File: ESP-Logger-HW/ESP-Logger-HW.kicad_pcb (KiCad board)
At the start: 2 copper layers, 2 parts

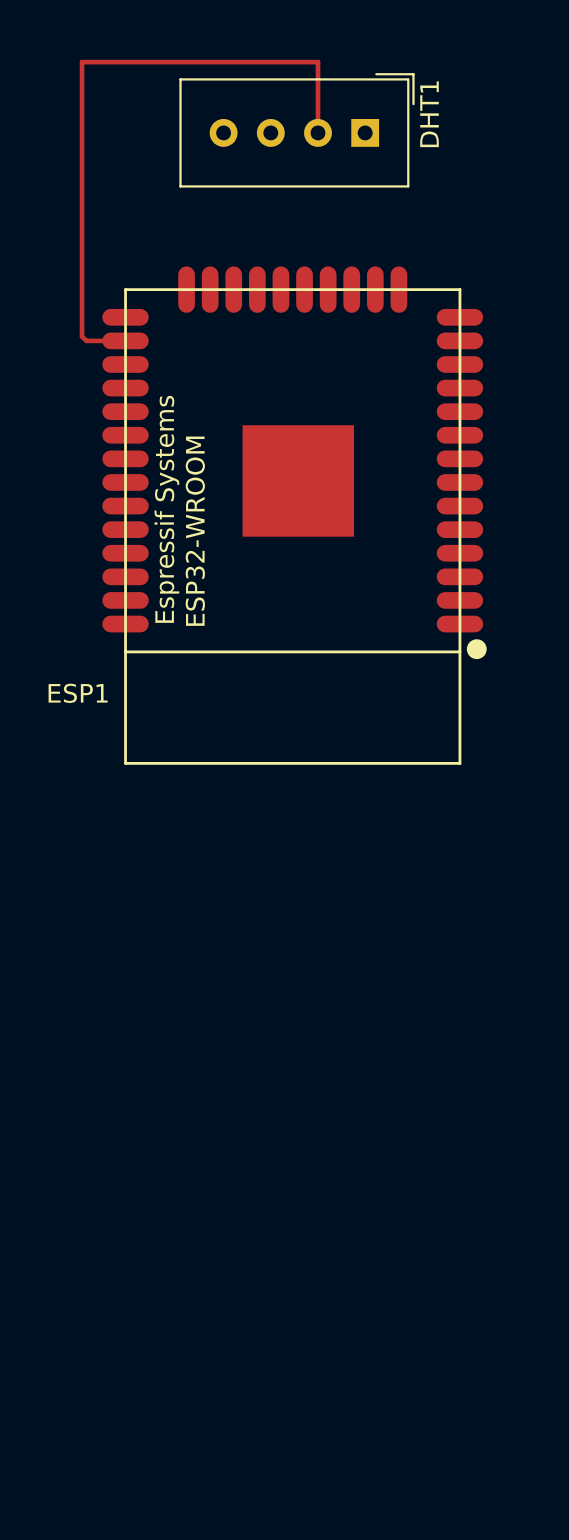
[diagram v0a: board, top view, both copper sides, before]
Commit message: First complete PCB
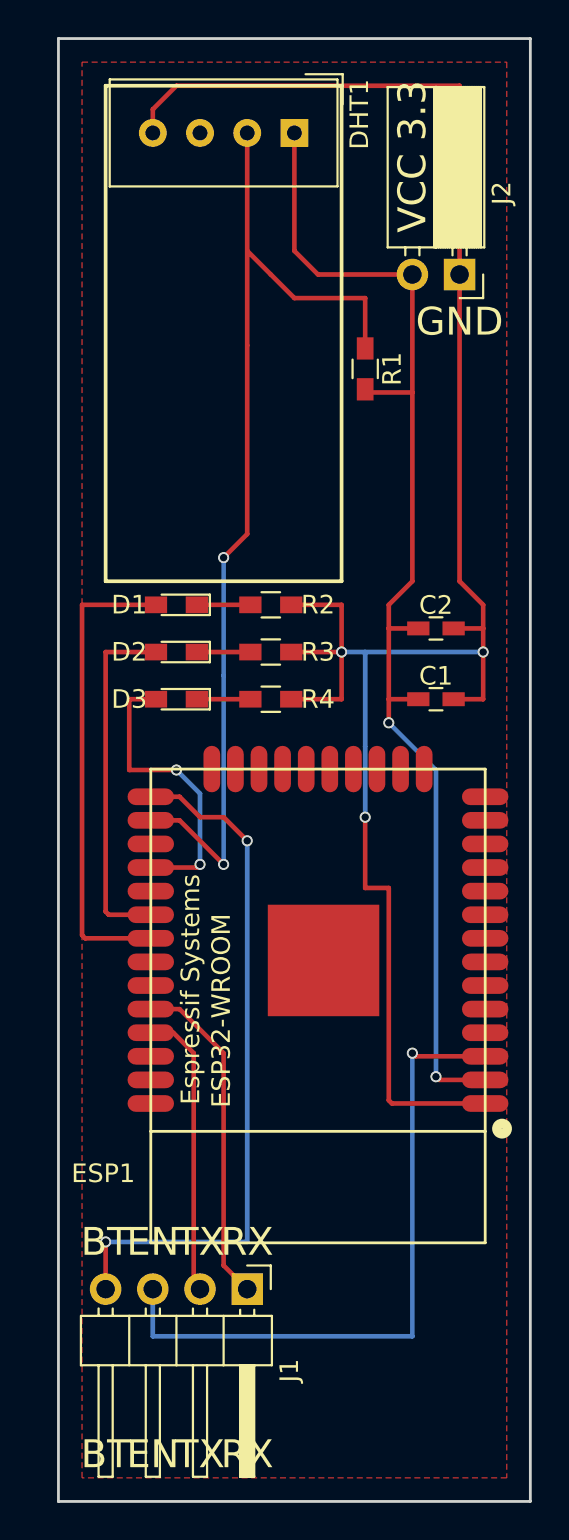
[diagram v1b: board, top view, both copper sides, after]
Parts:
- added C1: 0.1uF, Capacitors_SMD:C_0603_HandSoldering, F.Cu at (58.4, 62.2)
- added C2: 10uF, Capacitors_SMD:C_0603_HandSoldering, F.Cu at (58.4, 58.4)
- added D1: LED, LEDs:LED_0603_HandSoldering, F.Cu at (44.5, 57.1)
- added D2: LED, LEDs:LED_0603_HandSoldering, F.Cu at (44.5, 59.7)
- added D3: LED, LEDs:LED_0603_HandSoldering, F.Cu at (44.5, 62.2)
- added J1: Conn_01x04_Male, Pin_Headers:Pin_Header_Angled_1x04_Pitch2.54mm, F.Cu at (48.3, 94.0)
- added J2: Conn_01x02_Female, Socket_Strips:Socket_Strip_Angled_1x02_Pitch2.54mm, F.Cu at (59.7, 39.4)
- added R1: 1K, Resistors_SMD:R_0603_HandSoldering, F.Cu at (54.6, 44.5)
- added R2: 220, Resistors_SMD:R_0603_HandSoldering, F.Cu at (49.5, 57.1)
- added R3: 220, Resistors_SMD:R_0603_HandSoldering, F.Cu at (49.5, 59.7)
- added R4: 220, Resistors_SMD:R_0603_HandSoldering, F.Cu at (49.5, 62.2)
- moved ESP1 25.8 mm to (52.1, 78.7)
- moved DHT1 3.81 mm to (50.8, 31.8)
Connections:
- ESP1 pad 25: Net-(ESP1-Pad25) -> /BOOT
- ESP1 pad 39: Net-(ESP1-Pad39) -> GND
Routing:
- net GND: track 0.00 -> 106.5 mm, vias 0 -> 3
- net VCC: track 0.00 -> 66.5 mm, vias 0 -> 2
- net /BOOT: track 0.00 -> 37.9 mm, vias 0 -> 2
- net Net-(ESP1-Pad3): track 0.00 -> 35.7 mm, vias 0 -> 1
- net Net-(D1-Pad2): track 0.00 -> 25.5 mm
- net Net-(DHT1-Pad2): track 33.7 -> 54.9 mm, vias 0 -> 2
- net Net-(D2-Pad2): track 0.00 -> 19.2 mm
- net Net-(ESP1-Pad34): track 0.00 -> 18.1 mm
- net Net-(D3-Pad2): track 0.00 -> 16.1 mm, vias 0 -> 2
- net Net-(ESP1-Pad35): track 0.00 -> 15.6 mm
- net Net-(D3-Pad1): track 0.00 -> 2.88 mm
- net Net-(D2-Pad1): track 0.00 -> 2.88 mm
- net Net-(D1-Pad1): track 0.00 -> 2.88 mm
- added copper zone on F.Cu, net GND
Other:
- board outline added: 25.4 x 78.7 mm
- rule pad_to_mask_clearance: 0.2 -> 0.1
- rule trace_min: 0.2 -> 0.25
- board text added: "BT"
- board text added: "EN"
- board text added: "GND"
- board text added: "RX"
- board text added: "TX"
- board text added: "VCC 3.3"

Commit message: Update the Pcb: Added the RC-Delay circuit that I forgot on the first prototype
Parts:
- added C3: 1uF, Capacitors_SMD:C_0603_HandSoldering, F.Cu at (61.0, 52.1)
- added R5: 10K, Resistors_SMD:R_0603_HandSoldering, F.Cu at (55.9, 52.1)
- J1: footprint Pin_Headers:Pin_Header_Angled_1x04_Pitch2.54mm -> Connectors_JST:JST_XH_B04B-XH-A_04x2.50mm_Straight
- J2: footprint Socket_Strips:Socket_Strip_Angled_1x02_Pitch2.54mm -> Connectors_JST:JST_XH_B02B-XH-A_02x2.50mm_Straight
- moved J1 10.1 mm to (58.3, 95.2), turned to 180 degrees
- moved J2 3.81 mm to (59.7, 35.6), turned to 180 degrees
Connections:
- net /BOOT renamed Net-(ESP1-Pad25)
- ESP1 pad 38: Net-(ESP1-Pad38) -> GND
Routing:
- net GND: track 106.5 -> 161.4 mm
- net Net-(C3-Pad1): track 35.7 -> 68.7 mm, vias 1 -> 5
- net Net-(ESP1-Pad34): track 18.1 -> 32.0 mm, vias 0 -> 3
- net Net-(ESP1-Pad35): track 15.6 -> 29.4 mm, vias 0 -> 4
- net Net-(ESP1-Pad25): track 37.9 -> 31.9 mm, vias 2 -> 0
- net VCC: track 66.5 -> 71.7 mm
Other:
- board size 25.4 x 78.7 mm -> 25.4 x 73.7 mm

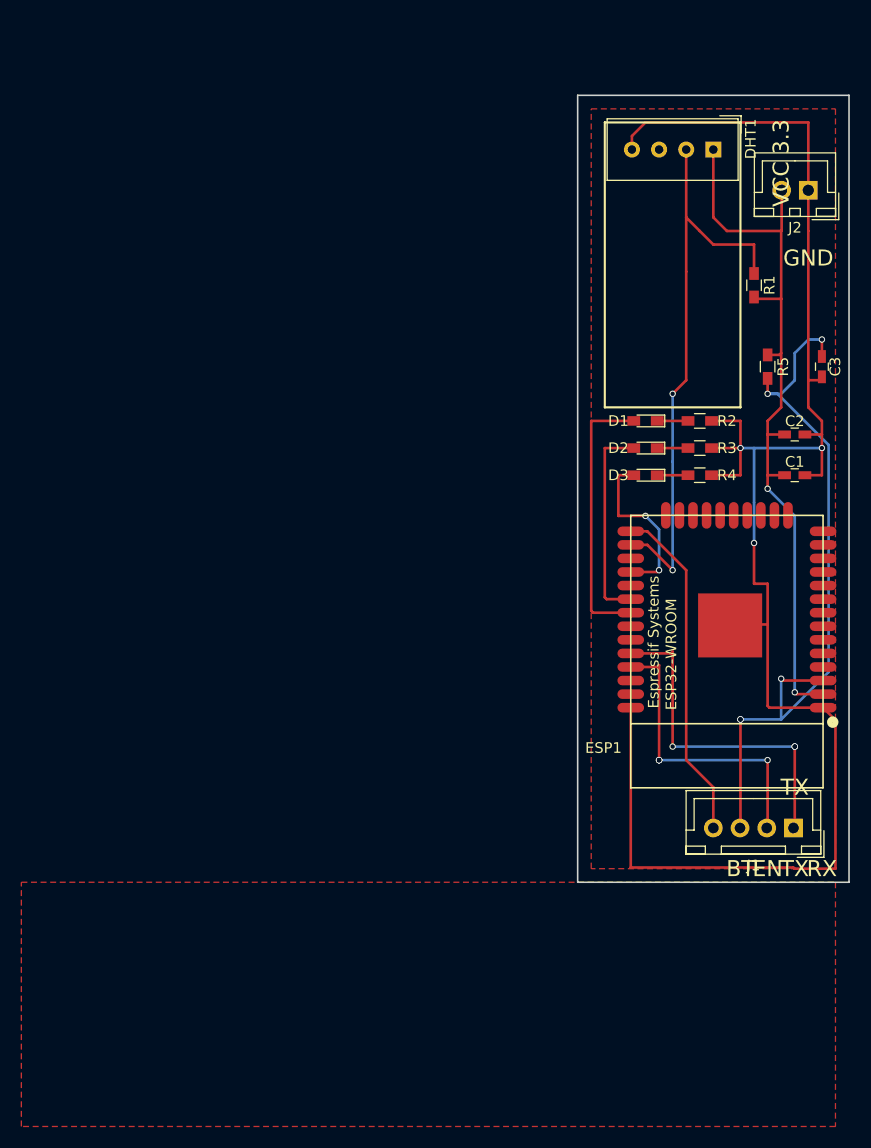
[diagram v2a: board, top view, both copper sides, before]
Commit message: New 30x40 mm small Pcb layout
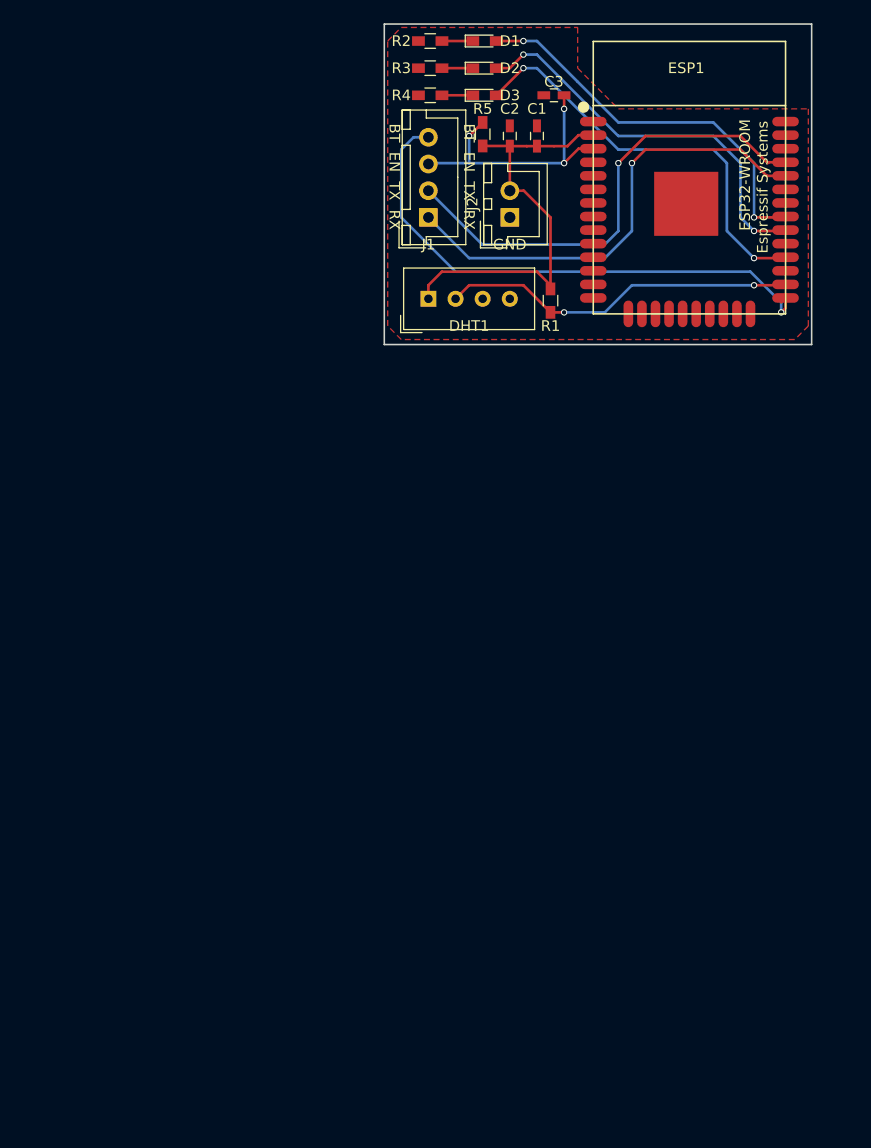
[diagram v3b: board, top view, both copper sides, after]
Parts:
- moved J1 66.6 mm to (24.1, 38.1), turned to 90 degrees
- moved ESP1 44.5 mm to (48.6, 34.4), turned to 180 degrees
- moved R2 43.6 mm to (24.3, 21.6), turned to 180 degrees
- moved R3 43.6 mm to (24.3, 24.1), turned to 180 degrees
- moved R4 43.6 mm to (24.3, 26.7), turned to 180 degrees
- moved C1 39.9 mm to (34.3, 30.5), turned to 90 degrees
- moved C2 38.6 mm to (31.8, 30.5), turned to 90 degrees
- moved D1 38.6 mm to (29.4, 21.6), turned to 0 degrees
- moved D2 38.6 mm to (29.4, 24.1), turned to 0 degrees
- moved D3 38.6 mm to (29.4, 26.7), turned to 0 degrees
- moved C3 35.7 mm to (35.9, 26.7), turned to 180 degrees
- moved R5 34.4 mm to (29.2, 30.3), turned to 90 degrees
- moved DHT1 30.1 mm to (24.1, 45.7), turned to 90 degrees
- moved J2 28.1 mm to (31.8, 38.1), turned to 90 degrees
- moved R1 19.1 mm to (35.6, 45.9), turned to 90 degrees
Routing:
- net GND: track 161.4 -> 0.43 mm, vias 3 -> 0
- net Net-(C3-Pad1): track 68.7 -> 26.8 mm, vias 5 -> 3
- net VCC: track 71.7 -> 40.6 mm, vias 2 -> 0
- net Net-(D3-Pad2): track 16.1 -> 39.2 mm
- net Net-(DHT1-Pad2): track 54.9 -> 33.6 mm
- net Net-(ESP1-Pad25): track 31.9 -> 51.3 mm, vias 0 -> 1
- net Net-(D2-Pad2): track 19.2 -> 37.5 mm, vias 0 -> 2
- net Net-(ESP1-Pad35): track 29.4 -> 44.5 mm, vias 4 -> 1
- net Net-(ESP1-Pad34): track 32.0 -> 44.0 mm, vias 3 -> 1
- net Net-(D1-Pad2): track 25.5 -> 36.9 mm, vias 0 -> 2
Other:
- board size 25.4 x 73.7 mm -> 40 x 30 mm
- board text added: "BT EN TX RX"
- board text removed: "BT"
- board text removed: "EN"
- board text removed: "RX"
- board text removed: "TX"
- board text removed: "VCC 3.3"

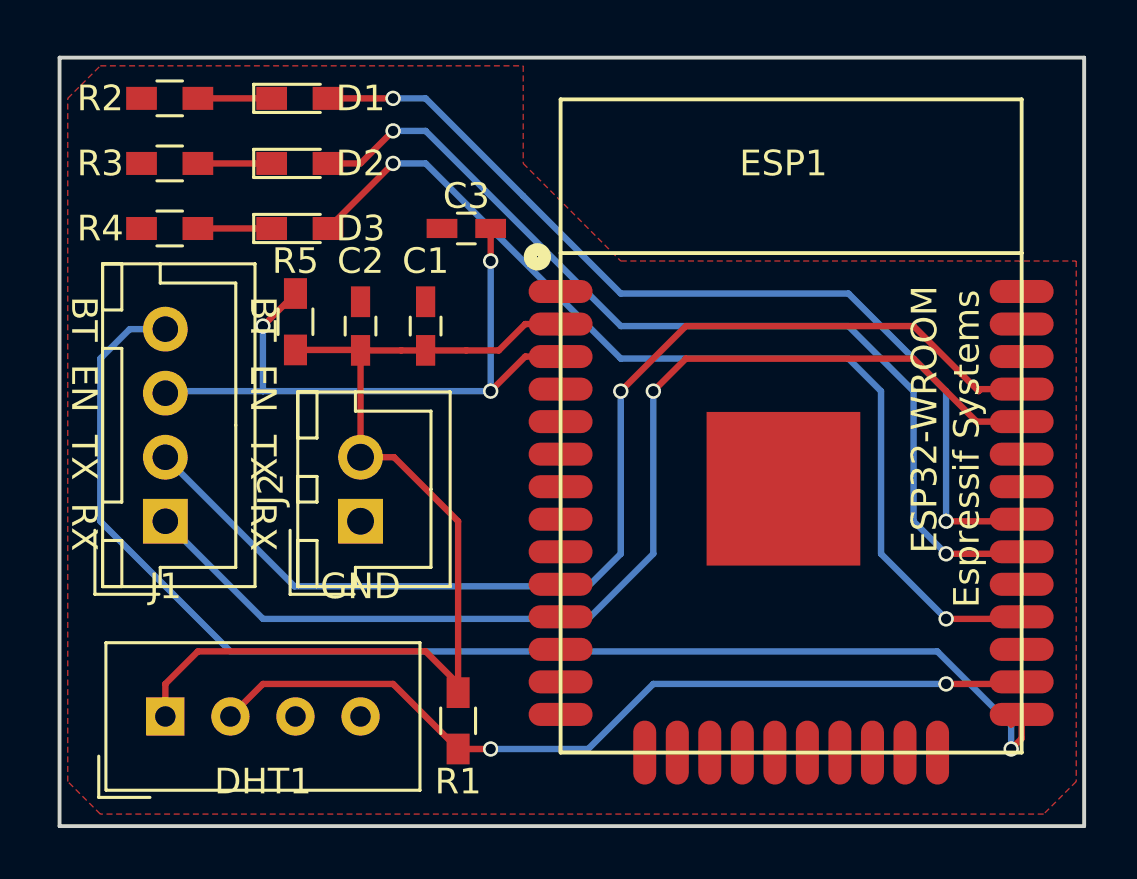
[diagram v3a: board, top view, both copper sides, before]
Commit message: Update PCB and Gerber: Add USB power supply and voltage regulator
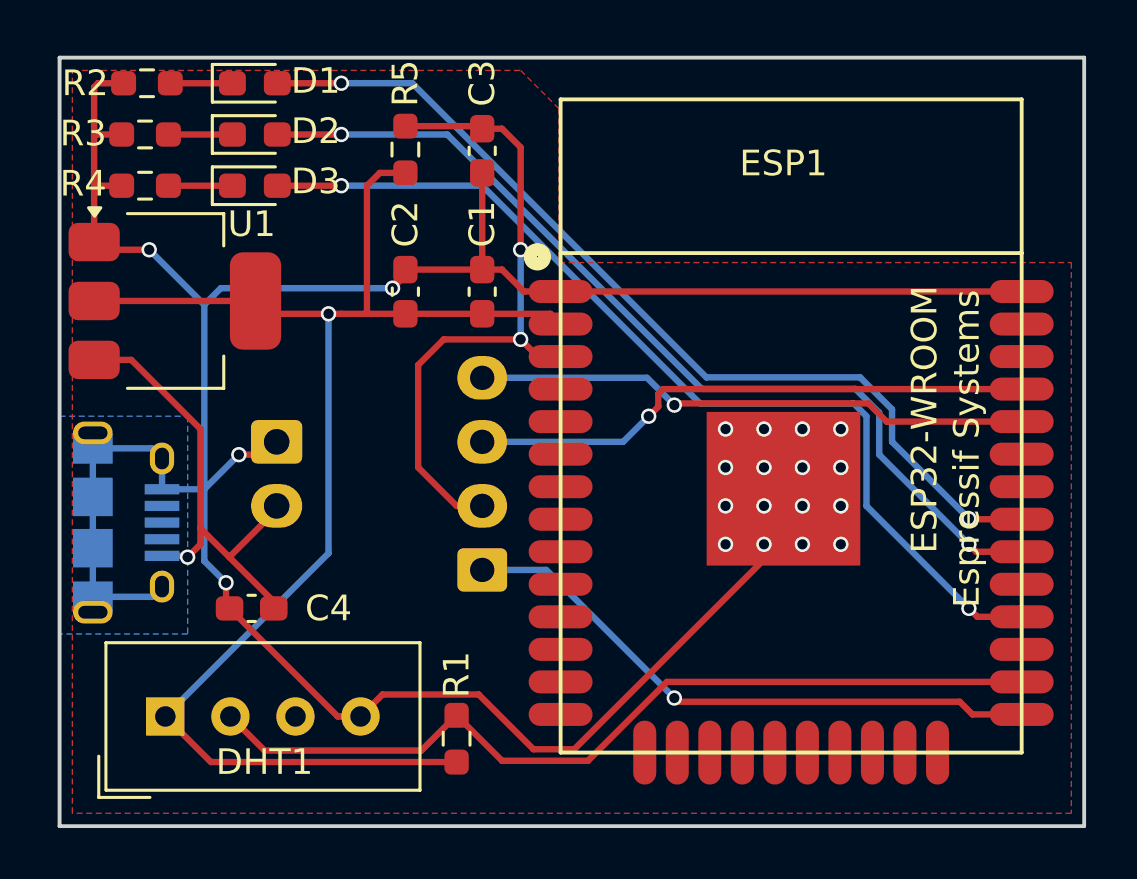
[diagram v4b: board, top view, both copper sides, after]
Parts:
- added C4: 0.1uF, Capacitor_SMD:C_0603_1608Metric_Pad1.08x0.95mm_HandSolder, F.Cu at (27.5, 41.5)
- added J3: USB, Connector_USB:USB_Micro-B_Amphenol_10118194_Horizontal, B.Cu at (22.6, 38.1)
- added U1: LD33V, Package_TO_SOT_SMD:SOT-223-3_TabPin2, F.Cu at (24.5, 29.5)
- C1, C2, C3: footprint Capacitors_SMD:C_0603_HandSoldering -> Capacitor_SMD:C_0603_1608Metric_Pad1.08x0.95mm_HandSolder
- D1, D2, D3: footprint LEDs:LED_0603_HandSoldering -> LED_SMD:LED_0603_1608Metric_Pad1.05x0.95mm_HandSolder
- J1: footprint Connectors_JST:JST_XH_B04B-XH-A_04x2.50mm_Straight -> Connector_JST:JST_XH_B4B-XH-A_1x04_P2.50mm_Vertical; moved to B.Cu
- J2: value Conn_01x02_Female -> PWR; footprint Connectors_JST:JST_XH_B02B-XH-A_02x2.50mm_Straight -> Connector_JST:JST_XH_B2B-XH-A_1x02_P2.50mm_Vertical; moved to B.Cu
- R1, R2, R3, R4, R5: footprint Resistors_SMD:R_0603_HandSoldering -> Resistor_SMD:R_0603_1608Metric_Pad0.98x0.95mm_HandSolder
- moved J1 12.5 mm to (36.5, 40.0)
- moved R5 7.97 mm to (33.5, 23.6)
- moved J2 4.51 mm to (28.5, 35.0), turned to -90 degrees
- moved C3 3.10 mm to (36.5, 23.6), turned to -90 degrees
- moved C1 2.59 mm to (36.5, 29.1)
- moved D3 2.42 mm to (27.6, 25.0)
- moved C2 2.21 mm to (33.5, 29.1)
- moved D2 2.09 mm to (27.6, 23.0)
- moved R4 1.93 mm to (23.3, 25.0)
- moved D1 1.85 mm to (27.6, 21.0)
- moved R3 1.48 mm to (23.3, 23.0)
- moved R2 1.07 mm to (23.4, 21.0)
- moved R1 0.70 mm to (35.5, 46.6), turned to -90 degrees
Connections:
- C3 pad 1: Net-(C3-Pad1) -> Net-(ESP1-EN)
- DHT1 pad 3: Net-(DHT1-Pad3) -> unconnected-(DHT1-NC-Pad3)
- ESP1 pad 10: Net-(ESP1-Pad10) -> unconnected-(ESP1-IO25-Pad10)
- ESP1 pad 11: Net-(ESP1-Pad11) -> unconnected-(ESP1-IO26-Pad11)
- ESP1 pad 12: Net-(ESP1-Pad12) -> unconnected-(ESP1-IO27-Pad12)
- ESP1 pad 13: Net-(ESP1-Pad13) -> unconnected-(ESP1-IO14-Pad13)
- ESP1 pad 14: Net-(ESP1-Pad14) -> unconnected-(ESP1-IO12-Pad14)
- ESP1 pad 15: Net-(ESP1-Pad15) -> unconnected-(ESP1-GND-Pad15)
- ESP1 pad 16: Net-(ESP1-Pad16) -> unconnected-(ESP1-IO13-Pad16)
- ESP1 pad 17: Net-(ESP1-Pad17) -> unconnected-(ESP1-SD2-Pad17)
- ESP1 pad 18: Net-(ESP1-Pad18) -> unconnected-(ESP1-SD3-Pad18)
- ESP1 pad 19: Net-(ESP1-Pad19) -> unconnected-(ESP1-CMD-Pad19)
- ESP1 pad 20: Net-(ESP1-Pad20) -> unconnected-(ESP1-CLK-Pad20)
- ESP1 pad 21: Net-(ESP1-Pad21) -> unconnected-(ESP1-SDO-Pad21)
- ESP1 pad 22: Net-(ESP1-Pad22) -> unconnected-(ESP1-SD1-Pad22)
- ESP1 pad 23: Net-(ESP1-Pad23) -> unconnected-(ESP1-IO15-Pad23)
- ESP1 pad 24: Net-(ESP1-Pad24) -> unconnected-(ESP1-IO2-Pad24)
- ESP1 pad 25: Net-(ESP1-Pad25) -> Net-(ESP1-IO0)
- ESP1 pad 27: Net-(ESP1-Pad27) -> unconnected-(ESP1-IO16-Pad27)
- ESP1 pad 29: Net-(ESP1-Pad29) -> unconnected-(ESP1-IO5-Pad29)
- ESP1 pad 3: Net-(C3-Pad1) -> Net-(ESP1-EN)
- ESP1 pad 32: Net-(ESP1-Pad32) -> unconnected-(ESP1-NC-Pad32)
- ESP1 pad 33: Net-(ESP1-Pad33) -> unconnected-(ESP1-IO21-Pad33)
- ESP1 pad 34: Net-(ESP1-Pad34) -> Net-(ESP1-RXD0)
- ESP1 pad 35: Net-(ESP1-Pad35) -> Net-(ESP1-TXD0)
- ESP1 pad 36: Net-(ESP1-Pad36) -> unconnected-(ESP1-IO22-Pad36)
- ESP1 pad 37: Net-(ESP1-Pad37) -> unconnected-(ESP1-IO23-Pad37)
- ESP1 pad 4: Net-(ESP1-Pad4) -> unconnected-(ESP1-SENSOR_VP-Pad4)
- ESP1 pad 5: Net-(ESP1-Pad5) -> unconnected-(ESP1-SENSOR_VN-Pad5)
- ESP1 pad 6: Net-(ESP1-Pad6) -> unconnected-(ESP1-IO34-Pad6)
- ESP1 pad 7: Net-(ESP1-Pad7) -> unconnected-(ESP1-IO35-Pad7)
- ESP1 pad 8: Net-(ESP1-Pad8) -> unconnected-(ESP1-IO32-Pad8)
- ESP1 pad 9: Net-(ESP1-Pad9) -> unconnected-(ESP1-IO33-Pad9)
- J1 pad 1: Net-(ESP1-Pad34) -> Net-(ESP1-IO0)
- J1 pad 2: Net-(ESP1-Pad35) -> Net-(ESP1-EN)
- J1 pad 3: Net-(C3-Pad1) -> Net-(ESP1-TXD0)
- J1 pad 4: Net-(ESP1-Pad25) -> Net-(ESP1-RXD0)
- J2 pad 2: VCC -> Net-(J2-Pin_2)
- R5 pad 2: Net-(C3-Pad1) -> Net-(ESP1-EN)
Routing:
- net GND: track 0.43 -> 115.1 mm, vias 0 -> 20
- net Net-(ESP1-Pad25): track 51.3 -> 0.00 mm, vias 1 -> 0
- net Net-(ESP1-Pad35): track 44.5 -> 0.00 mm, vias 1 -> 0
- net Net-(ESP1-Pad34): track 44.0 -> 0.00 mm, vias 1 -> 0
- net Net-(C3-Pad1): track 26.8 -> 0.00 mm, vias 3 -> 0
- net Net-(ESP1-EN): track 0.00 -> 25.7 mm, vias 0 -> 2
- net Net-(ESP1-IO0): track 0.00 -> 23.4 mm, vias 0 -> 1
- net Net-(ESP1-TXD0): track 0.00 -> 22.2 mm, vias 0 -> 1
- net Net-(ESP1-RXD0): track 0.00 -> 21.8 mm, vias 0 -> 1
- net Net-(J2-Pin_2): track 0.00 -> 18.6 mm, vias 0 -> 1
- net VCC: track 40.6 -> 55.8 mm, vias 0 -> 1
- net Net-(D3-A): track 39.2 -> 38.1 mm
- net Net-(D2-A): track 37.5 -> 36.8 mm
- net Net-(DHT1-IO): track 33.6 -> 34.0 mm, vias 2 -> 0
- added copper zone on B.Cu, net GND
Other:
- net class Default removed
- board text removed: "BT EN TX RX"
